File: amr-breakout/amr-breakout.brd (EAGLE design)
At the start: 55 x 50 mm, 15 parts, among them U1 ZLDO1117G33TC

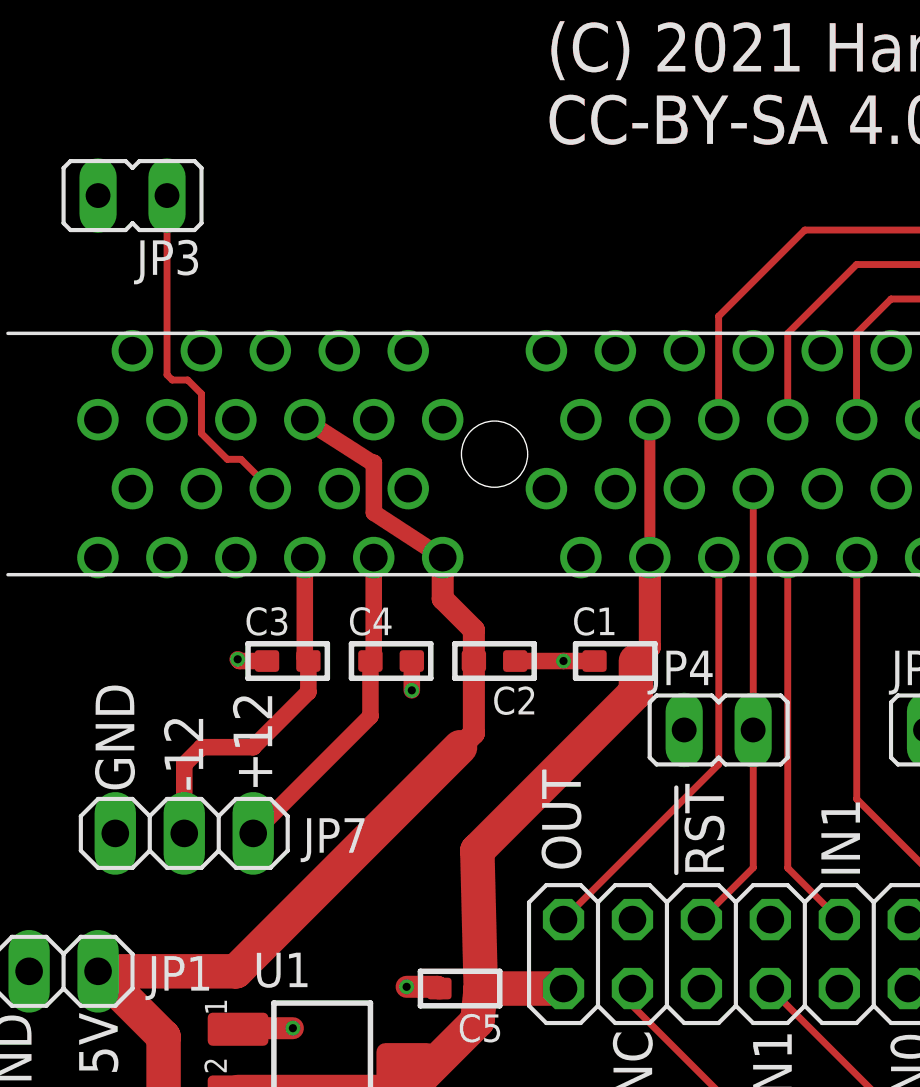
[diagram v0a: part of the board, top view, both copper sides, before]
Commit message: amr-breakout: Add pull-ups for !AC97_RESET and !PRIMARY_DN
Closes: OS#5369
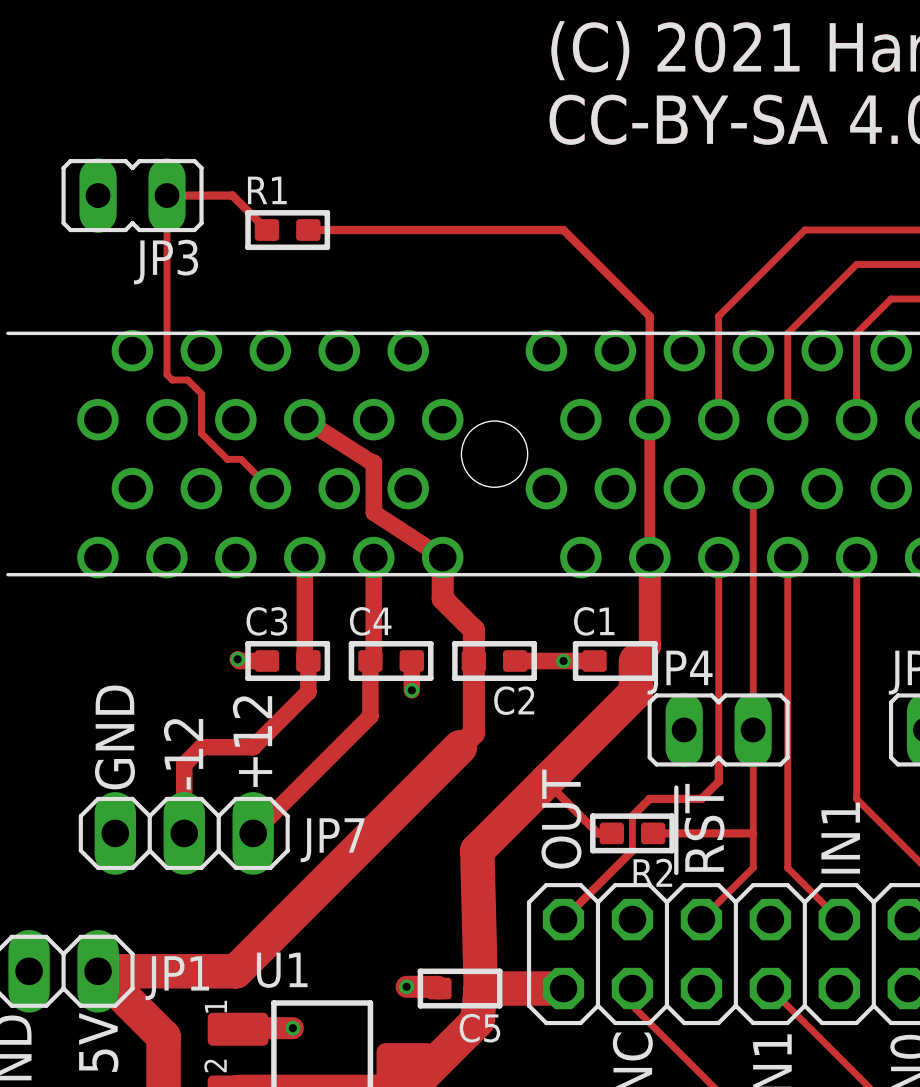
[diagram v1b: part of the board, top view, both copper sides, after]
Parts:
- added R1, R2: 10k, rc-sysmocom:_0603
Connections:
- net !AC97_RESET: now also R2.1
- net !PRIMARY_DN: now also R1.1
- net VCC: now also R1.2, R2.2
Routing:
- net VCC: track 41.7 -> 62.6 mm
- net !PRIMARY_DN: track 13.0 -> 17.2 mm
- net !AC97_RESET: track 17.3 -> 21.0 mm
- net AC97_SDATA_OUT: track 15.7 -> 16.8 mm
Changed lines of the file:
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@@
 <attribute name="VALUE" x="5.08" y="13.97" size="1.27" layer="27"/>
 </element>
+<element name="R1" library="rc-sysmocom" package="_0603" value="10k" x="12.7" y="39.37"/>
+<element name="R2" library="rc-sysmocom" package="_0603" value="10k" x="25.4" y="17.145" rot="R180"/>
 </elements>
 <signals>
@@
 <wire x1="26.04" y1="24.008" x2="25.527" y2="23.495" width="0.8128" layer="1"/>
 <wire x1="25.527" y1="23.495" x2="25.527" y2="22.352" width="1.27" layer="1"/>
-<wire x1="25.527" y1="22.352" x2="19.685" y2="16.51" width="1.27" layer="1"/>
+<wire x1="25.527" y1="22.352" x2="22.225" y2="19.05" width="1.27" layer="1"/>
+<wire x1="22.225" y1="19.05" x2="19.685" y2="16.51" width="1.27" layer="1"/>
 <wire x1="19.685" y1="16.51" x2="19.812" y2="11.43" width="1.27" layer="1"/>
 <wire x1="10.8712" y1="7.62" x2="17.069" y2="7.62" width="1.27" layer="1"/>
+<contactref element="R1" pad="2"/>
+<contactref element="R2" pad="2"/>
+<wire x1="13.462" y1="39.37" x2="22.86" y2="39.37" width="0.3048" layer="1"/>
+<wire x1="22.86" y1="39.37" x2="26.035" y2="36.195" width="0.3048" layer="1"/>
+<wire x1="26.035" y1="36.195" x2="26.035" y2="32.39" width="0.3048" layer="1"/>
+<wire x1="26.035" y1="32.39" x2="26.04" y2="32.385" width="0.3048" layer="1"/>
+<wire x1="24.638" y1="17.145" x2="24.13" y2="17.145" width="0.3048" layer="1"/>
+<wire x1="24.13" y1="17.145" x2="22.225" y2="19.05" width="0.3048" layer="1"/>
 </signal>
 <signal name="-12V">
@@
 <contactref element="JP2" pad="2"/>
 <wire x1="28.58" y1="27.305" x2="28.58" y2="19.69" width="0.254" layer="1"/>
-<wire x1="28.58" y1="19.69" x2="22.86" y2="13.97" width="0.254" layer="1"/>
+<wire x1="28.58" y1="19.69" x2="28.58" y2="19.055" width="0.3048" layer="1"/>
+<wire x1="28.58" y1="19.055" x2="27.94" y2="18.415" width="0.3048" layer="1"/>
+<wire x1="27.94" y1="18.415" x2="26.035" y2="18.415" width="0.3048" layer="1"/>
+<wire x1="26.035" y1="18.415" x2="25.4" y2="17.78" width="0.3048" layer="1"/>
+<wire x1="25.4" y1="17.78" x2="25.4" y2="16.51" width="0.25" layer="1"/>
+<wire x1="25.4" y1="16.51" x2="22.86" y2="13.97" width="0.3048" layer="1"/>
 </signal>
 <signal name="AC97_SDATA_IN3">
@@
 <contactref element="JP2" pad="6"/>
 <wire x1="29.85" y1="29.845" x2="29.85" y2="20.32" width="0.254" layer="1"/>
-<wire x1="29.85" y1="20.32" x2="29.85" y2="15.88" width="0.254" layer="1"/>
+<wire x1="29.85" y1="20.32" x2="29.85" y2="17.145" width="0.254" layer="1"/>
+<wire x1="29.85" y1="17.145" x2="29.85" y2="15.88" width="0.254" layer="1"/>
 <wire x1="29.85" y1="15.88" x2="27.94" y2="13.97" width="0.254" layer="1"/>
 <wire x1="29.845" y1="20.955" x2="29.85" y2="20.32" width="0.15" layer="1"/>
+<contactref element="R2" pad="1"/>
+<wire x1="26.162" y1="17.145" x2="29.85" y2="17.145" width="0.3048" layer="1"/>
 </signal>
 <signal name="!PRIMARY_DN">
@@
 <wire x1="8.4455" y1="33.8455" x2="8.255" y2="34.036" width="0.254" layer="1"/>
 <wire x1="8.255" y1="34.036" x2="8.255" y2="40.64" width="0.254" layer="1"/>
+<contactref element="R1" pad="1"/>
+<wire x1="8.255" y1="40.64" x2="10.668" y2="40.64" width="0.3048" layer="1"/>
+<wire x1="10.668" y1="40.64" x2="11.938" y2="39.37" width="0.3048" layer="1"/>
 </signal>
 <signal name="!AUDIO_MUTE">
